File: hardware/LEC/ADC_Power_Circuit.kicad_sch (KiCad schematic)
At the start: 10 parts, among them U6 MCP1501T-33E/CHY, U7 MCP1501T-33E/CHY, U8 LM2940CT-5.0/NOPB, U9 LM2940CT-5.0/NOPB

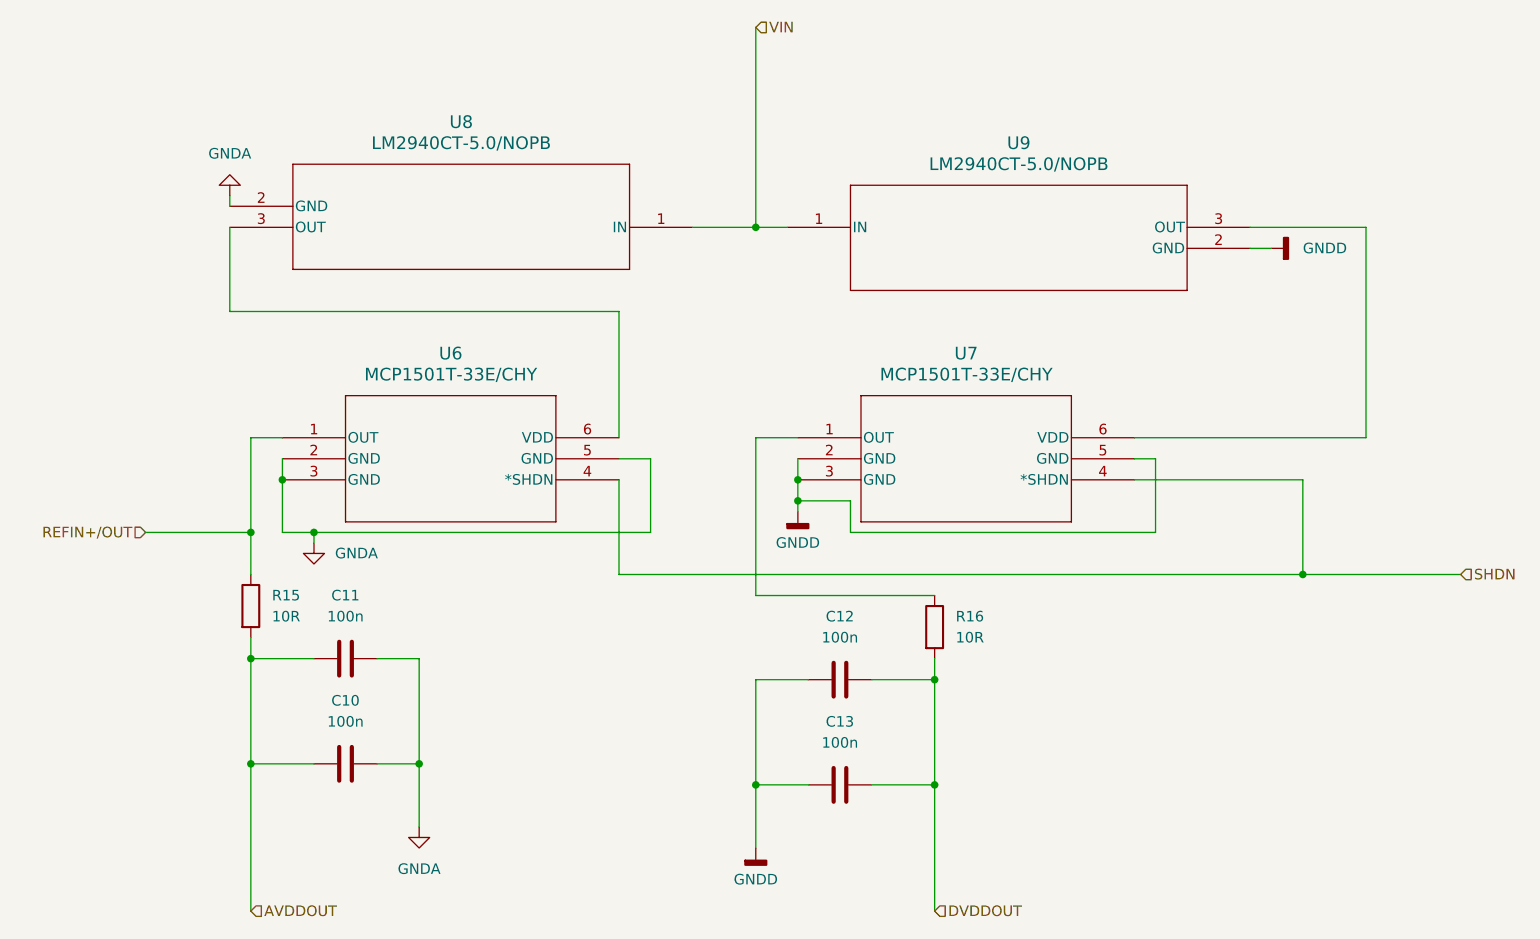
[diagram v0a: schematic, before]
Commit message: Updated LVR selection and other optimizations. Need to update footprints and symbols
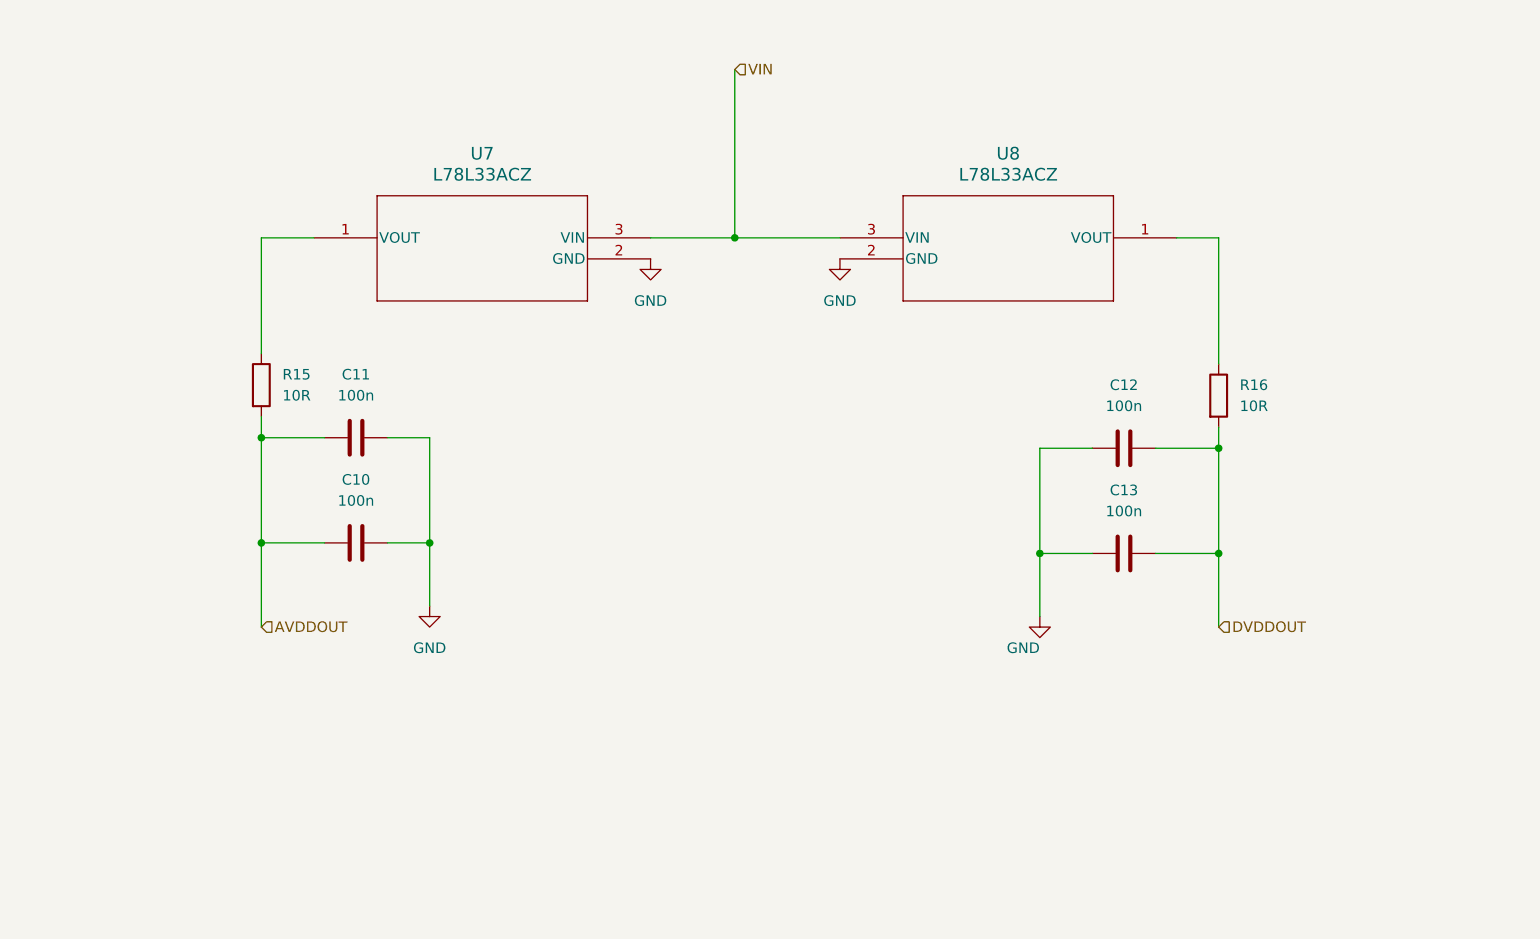
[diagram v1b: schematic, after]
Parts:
- removed U6, U7: MCP1501T-33E/CHY, SOT-23-6_CHY_MCH, symbol MCP1501T-33E/CHY:MCP1501T-33E_CHY
- removed U8, U9: LM2940CT-5.0/NOPB, T03B, symbol LM2940CT_5_0_NOPB:LM2940CT-5.0_NOPB
- added U7, U8: L78L33ACZ, L78L33ACZ:TO-92-TR_STM, symbol L78L33ACZ:L78L33ACZ
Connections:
- net GNDD is gone; now on net GND: C12.1, C13.1
- net VIN: now also U7.3 (VIN), U8.3 (VIN)
- net at R16.1: now also U8.1 (VOUT)
- net GNDA renamed GND
- net GND: now also U7.2 (GND), U8.2 (GND)
- net REFIN+/OUT: no longer names the net of R15.1
- net REFIN+/OUT: now also U7.1 (VOUT)
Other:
- moved on the sheet: C10, C11, C12, C13, R15, R16

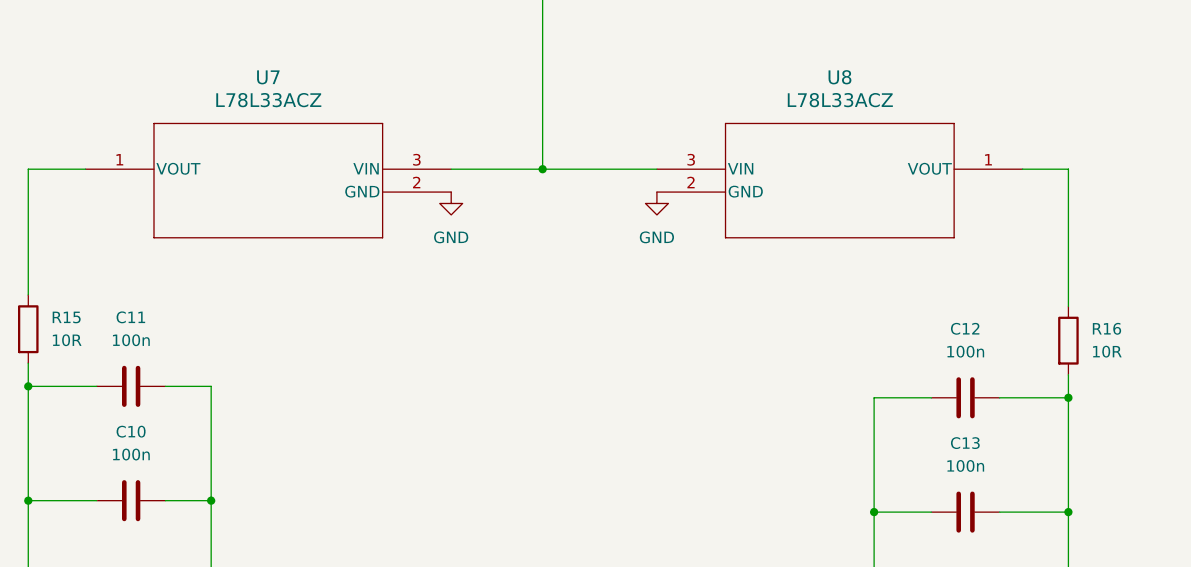
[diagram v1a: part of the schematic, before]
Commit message: Removed resistors on ADC power lines
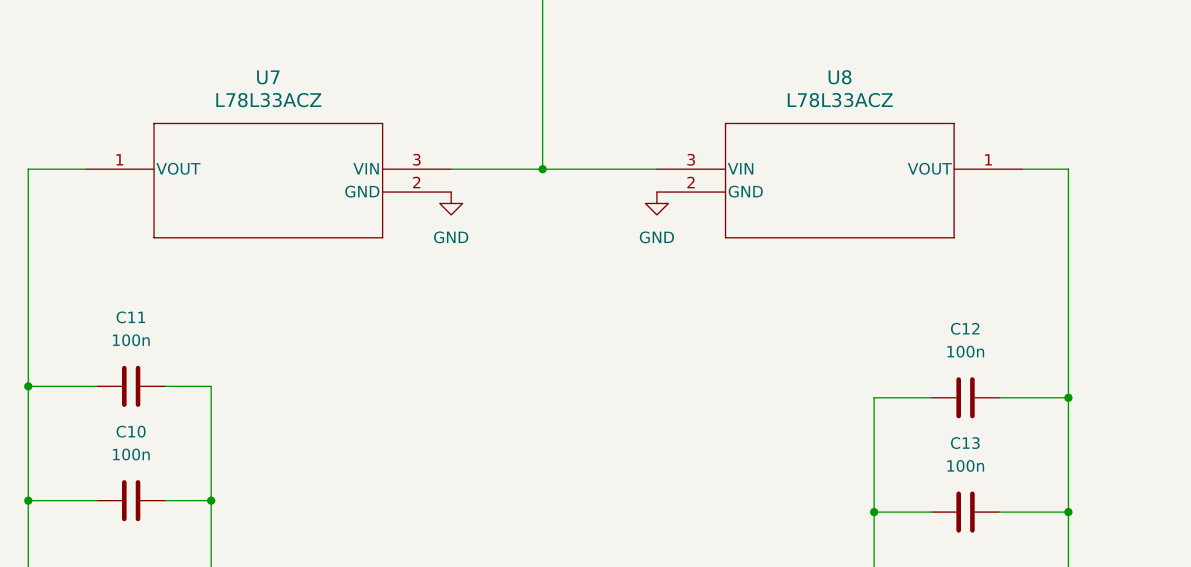
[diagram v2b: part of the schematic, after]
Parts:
- removed R15, R16: 10R, symbol Device:R
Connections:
- net AVDDOUT: now also U7.1 (VOUT)
- net DVDDOUT: now also U8.1 (VOUT)
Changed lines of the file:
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@@
     (stroke (width 0) (type default))
   )
-  (wire (pts (xy 91.44 92.71) (xy 91.44 95.25))
+  (wire (pts (xy 91.44 71.12) (xy 91.44 95.25))
     (stroke (width 0) (type default))
   )
@@
     (stroke (width 0) (type default))
   )
-  (wire (pts (xy 207.01 93.98) (xy 207.01 96.52))
+  (wire (pts (xy 207.01 71.12) (xy 207.01 96.52))
     (stroke (width 0) (type default))
   )
@@
     (stroke (width 0) (type default))
   )
-  (wire (pts (xy 207.01 71.12) (xy 207.01 86.36))
-    (stroke (width 0) (type default))
-  )
   (wire (pts (xy 207.01 109.22) (xy 207.01 118.11))
     (stroke (width 0) (type default))
@@
   )
   (wire (pts (xy 201.93 71.12) (xy 207.01 71.12))
-    (stroke (width 0) (type default))
-  )
-  (wire (pts (xy 91.44 71.12) (xy 91.44 85.09))
     (stroke (width 0) (type default))
   )
@@
     )
   )
-  (symbol (lib_id "Device:R") (at 207.01 90.17 0) (unit 1)
-    (in_bom yes) (on_board yes) (dnp no) (fields_autoplaced)
-    (property "Reference" "R16" (at 209.55 88.9 0)
-      (effects (font (size 1.27 1.27)) (justify left))
-    )
-    (property "Value" "10R" (at 209.55 91.44 0)
-      (effects (font (size 1.27 1.27)) (justify left))
-    )
-    (property "Footprint" "" (at 205.232 90.17 90)
-      (effects (font (size 1.27 1.27)) hide)
-    )
-    (property "Datasheet" "~" (at 207.01 90.17 0)
-      (effects (font (size 1.27 1.27)) hide)
-    )
-    (pin "1")
-    (pin "2")
-    (instances
-      (project "LEC"
-        (path "/c984ce56-a2b4-4cda-8793-153280694173"
-          (reference "R16") (unit 1)
-        )
-        (path "/c984ce56-a2b4-4cda-8793-153280694173/38faafce-a9fd-44cb-ac78-8ab2a8d54629"
-          (reference "R18") (unit 1)
-        )
-      )
-    )
-  )
   (symbol (lib_id "Device:C") (at 195.58 96.52 90) (unit 1)
     (in_bom yes) (on_board yes) (dnp no) (fields_autoplaced)
@@
         )
       )
-    )
-  )
-  (symbol (lib_id "Device:R") (at 91.44 88.9 0) (unit 1)
-    (in_bom yes) (on_board yes) (dnp no) (fields_autoplaced)
-    (property "Reference" "R15" (at 93.98 87.63 0)
-      (effects (font (size 1.27 1.27)) (justify left))
-    )
-    (property "Value" "10R" (at 93.98 90.17 0)
-      (effects (font (size 1.27 1.27)) (justify left))
-    )
-    (property "Footprint" "" (at 89.662 88.9 90)
-      (effects (font (size 1.27 1.27)) hide)
-    )
-    (property "Datasheet" "~" (at 91.44 88.9 0)
-      (effects (font (size 1.27 1.27)) hide)
-    )
-    (pin "1")
-    (pin "2")
-    (instances
-      (project "LEC"
-        (path "/c984ce56-a2b4-4cda-8793-153280694173"
-          (reference "R15") (unit 1)
-        )
-        (path "/c984ce56-a2b4-4cda-8793-153280694173/38faafce-a9fd-44cb-ac78-8ab2a8d54629"
-          (reference "R17") (unit 1)
-        )
-      )

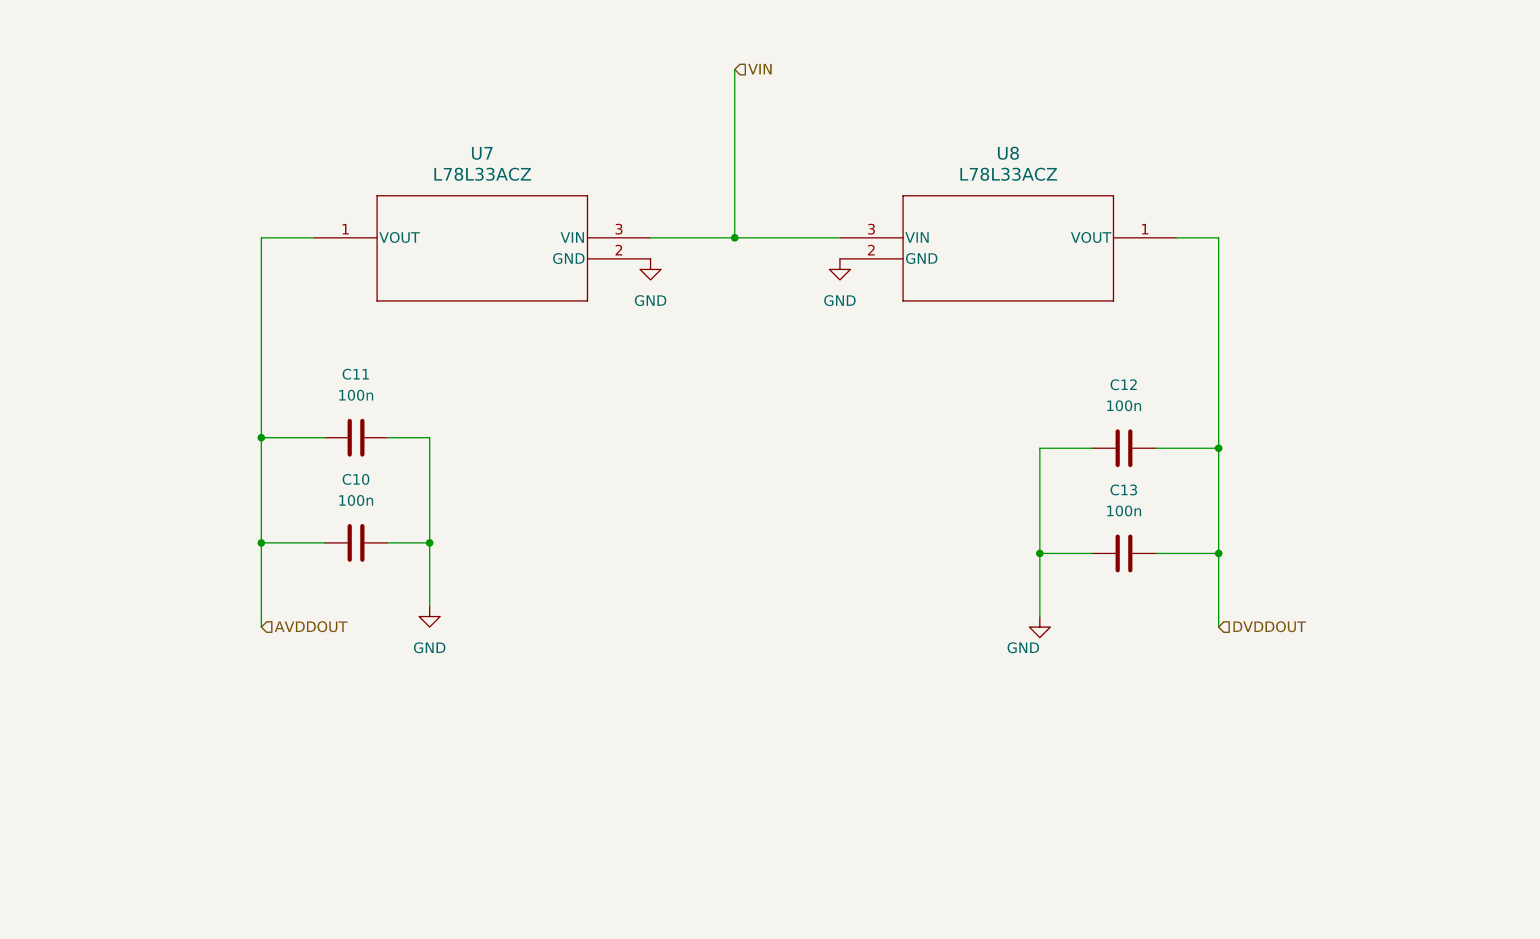
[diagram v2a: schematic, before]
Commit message: Added bulk capacitors to ADC LVRs, servos, and pico power inputs
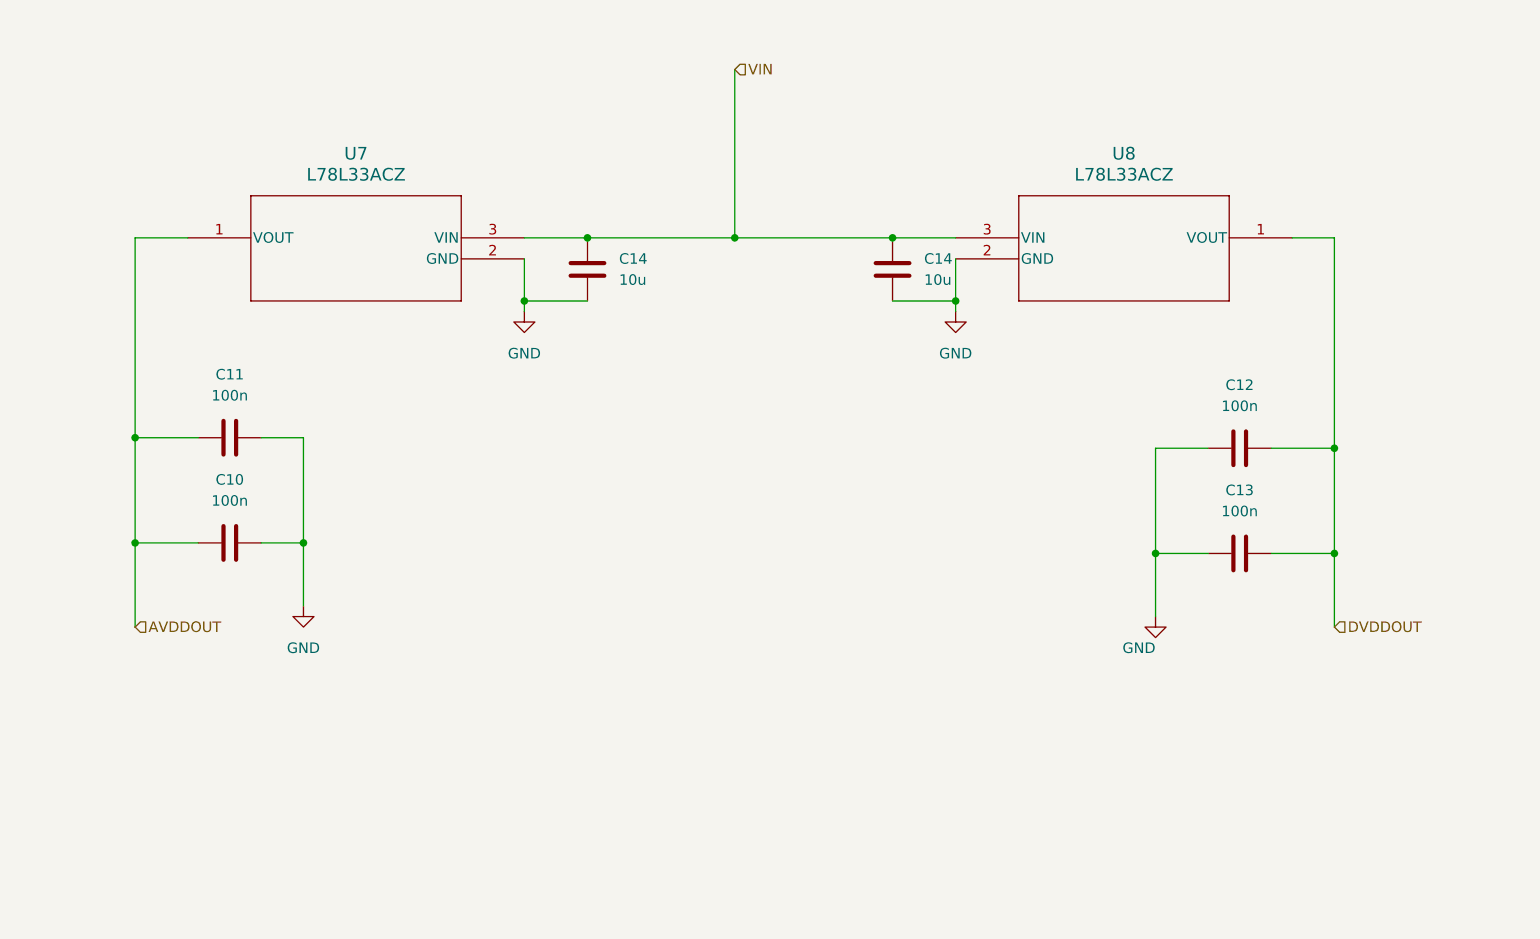
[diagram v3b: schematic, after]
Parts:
- added C14 (x2): 10u, symbol Device:C
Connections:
- net GND: now also C14.2, C14.2
- net VIN: now also C14.1, C14.1
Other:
- moved on the sheet: C10, C11, C12, C13, U7, U8

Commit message: Schematic done
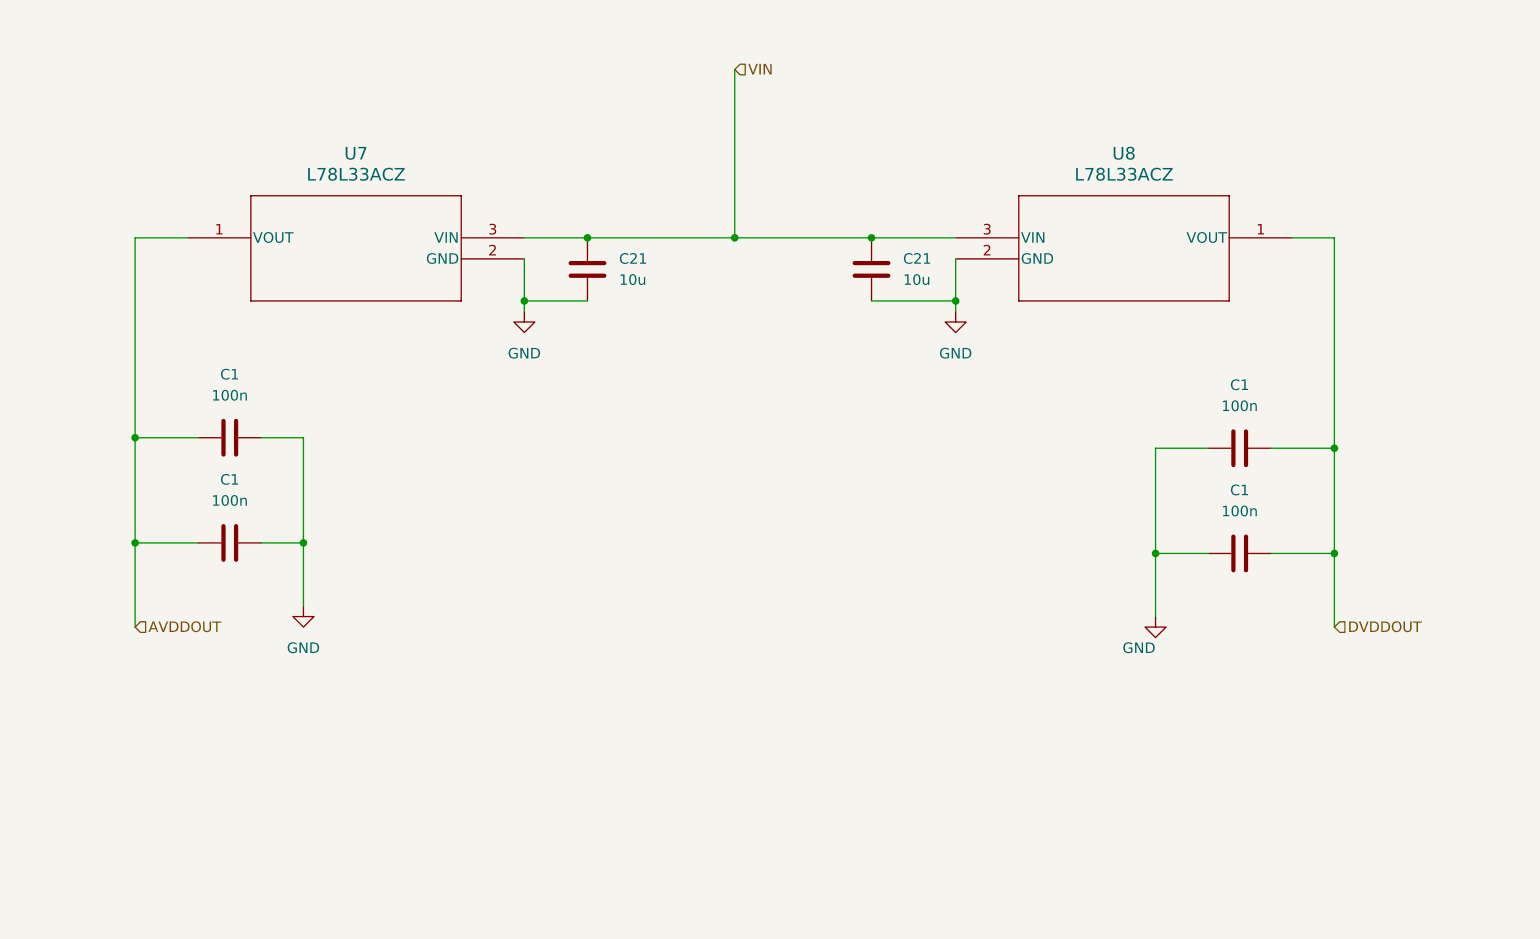
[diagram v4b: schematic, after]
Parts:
- removed C10, C11, C12, C13: 100n, symbol Device:C
- removed C14 (x2): 10u, symbol Device:C
- added C1 (x4): 100n, Capacitor_SMD:C_1206_3216Metric, symbol Device:C
- added C21 (x2): 10u, Capacitor_SMD:C_0805_2012Metric, symbol Device:C
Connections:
- net AVDDOUT: now also C1.1, C1.1
- net DVDDOUT: now also C1.2, C1.2
- net GND: now also C1.1, C1.1, C1.2, C1.2, C21.2, C21.2
- net VIN: now also C21.1, C21.1
